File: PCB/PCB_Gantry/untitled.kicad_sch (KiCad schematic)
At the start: 14 parts

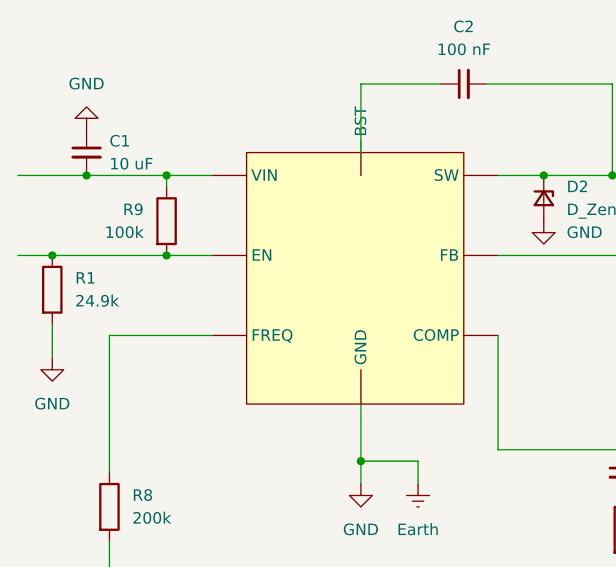
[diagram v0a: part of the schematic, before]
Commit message: Added Schematic
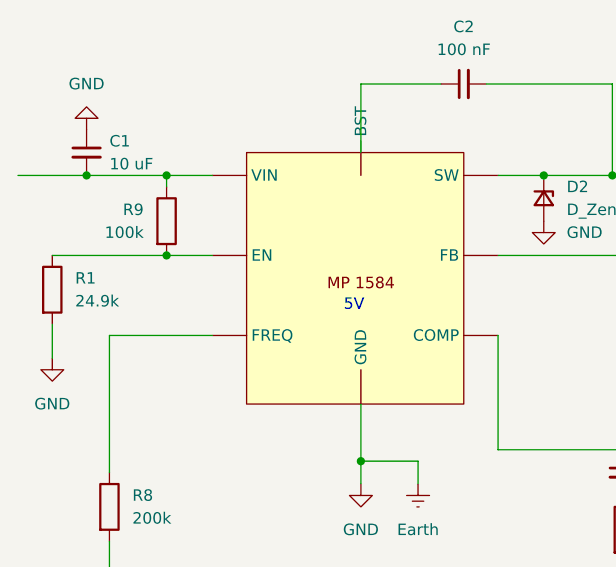
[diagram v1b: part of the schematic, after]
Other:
- note added: "5V"
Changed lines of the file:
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@@
 	(generator_version "9.0")
 	(paper "A4")
+	(text "5V"
+		(exclude_from_sim no)
+		(at 142.748 91.948 0)
+		(effects
+			(font
+				(size 1.27 1.27)
+			)
+		)
+	)
 	(text "MP 1584 5V"
 		(exclude_from_sim no)
@@
 	)
 	(junction
-		(at 109.22 86.36)
-		(diameter 0)
-		(color 0 0 0 0)
-	)
-	(junction
 		(at 205.74 77.47)
 		(diameter 0)
@@
 		(pts
 			(xy 158.75 86.36) (xy 173.99 86.36)
-		)
-		(stroke
-			(width 0)
-			(type default)
-		)
-	)
-	(wire
-		(pts
-			(xy 105.41 86.36) (xy 109.22 86.36)
 		)
 		(stroke
@@
 		)
 		(instances
-			(project "PCB_Gantry"
+			(project ""
 				(path "/018e7a75-50fa-45c9-b89e-77e71ddfff07/9d314bdc-1dcd-4bef-98ee-2bad15a320d8"
 					(reference "U1")
